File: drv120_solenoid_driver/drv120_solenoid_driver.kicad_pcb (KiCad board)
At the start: 2 copper layers, 9 parts, among them J1 Power, J2 Enable, J3 Solenoid, U1 drv120

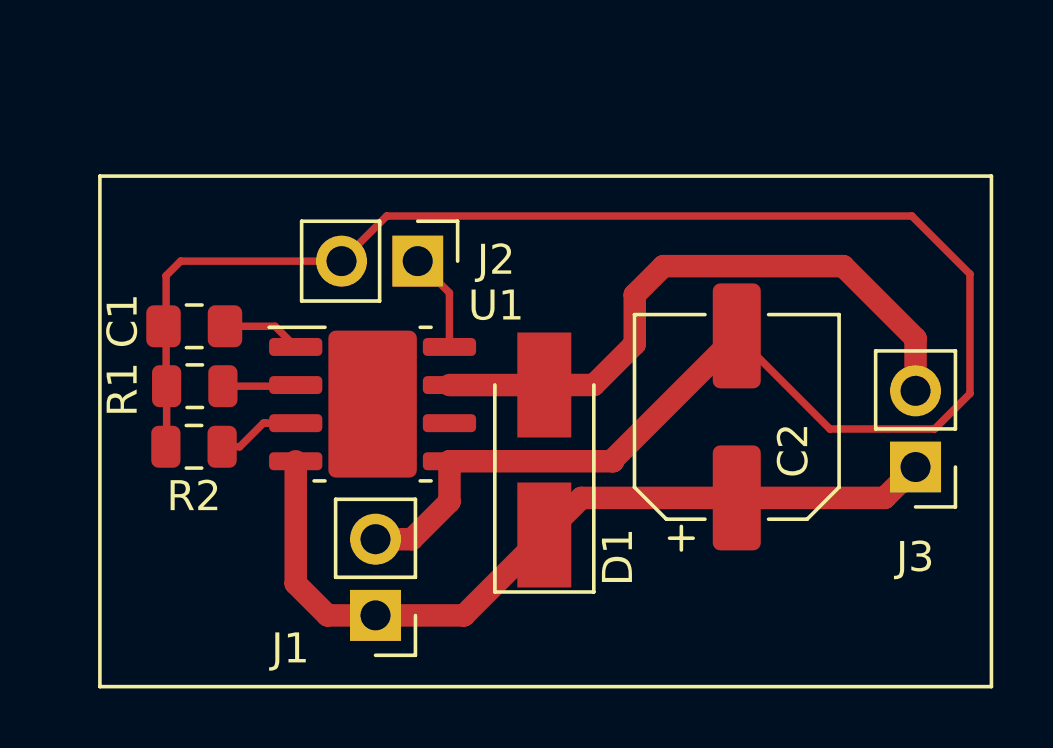
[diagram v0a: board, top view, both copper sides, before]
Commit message: Single sided for engraver
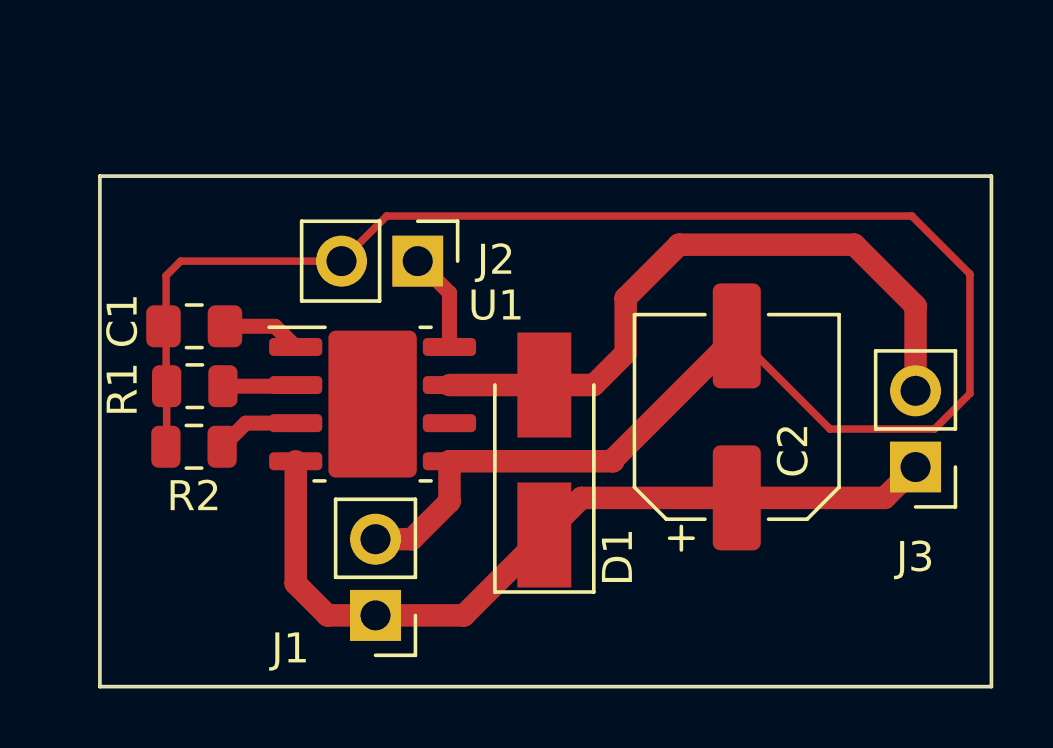
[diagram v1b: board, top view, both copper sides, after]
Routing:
- net Net-(C1-Pad1): track 2.73 -> 4.40 mm
- net Net-(D1-Pad2): track 20.9 -> 22.2 mm
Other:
- board outline added: 29.7 x 17 mm
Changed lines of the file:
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@@
   (general
     (thickness 1.6)
-    (drawings 4)
-    (tracks 48)
+    (drawings 8)
+    (tracks 47)
     (zones 0)
     (modules 9)
@@
   (layers
     (0 F.Cu signal)
-    (31 B.Cu signal)
-    (32 B.Adhes user)
-    (33 F.Adhes user)
-    (34 B.Paste user)
-    (35 F.Paste user)
+    (31 B.Cu signal hide)
+    (32 B.Adhes user hide)
+    (33 F.Adhes user hide)
+    (34 B.Paste user hide)
+    (35 F.Paste user hide)
     (36 B.SilkS user)
-    (37 F.SilkS user)
+    (37 F.SilkS user hide)
     (38 B.Mask user)
     (39 F.Mask user)
@@
   )
   (setup
-    (last_trace_width 0.25)
+    (last_trace_width 0.75)
     (user_trace_width 0.5)
     (user_trace_width 0.75)
@@
     (mod_text_size 1 1)
     (mod_text_width 0.15)
-    (pad_size 1.524 1.524)
-    (pad_drill 0.762)
+    (pad_size 3.5 1.6)
+    (pad_drill 0)
     (pad_to_mask_clearance 0.051)
     (solder_mask_min_width 0.25)
@@
     (visible_elements FFFFFF7F)
     (pcbplotparams
-      (layerselection 0x010fc_ffffffff)
+      (layerselection 0x01000_7fffffff)
       (usegerberextensions false)
       (usegerberattributes false)
@@
       (outputformat 1)
       (mirror false)
-      (drillshape 1)
+      (drillshape 0)
       (scaleselection 1)
-      (outputdirectory ""))
+      (outputdirectory "grbl/"))
   )
   (net 0 "")
@@
     (fp_line (start 3.3 -3.3) (end 3.3 3.3) (layer F.Fab) (width 0.1))
     (fp_circle (center 0 0) (end 3.15 0) (layer F.Fab) (width 0.1))
-    (pad 2 smd roundrect (at 2.7 0 90) (size 3.5 1.6) (layers F.Cu F.Paste F.Mask) (roundrect_rratio 0.15625)
-      (net 2 GND))
+    (pad 2 smd roundrect (at 2.7 0 90) (size 3.5 1.6) (layers F.Cu F.Paste F.Mask) (roundrect_rratio 0.156)
+      (net 2 GND) (zone_connect 2))
     (pad 1 smd roundrect (at -2.7 0 90) (size 3.5 1.6) (layers F.Cu F.Paste F.Mask) (roundrect_rratio 0.15625)
       (net 8 "Net-(C2-Pad1)"))
@@
     (fp_line (start -1 -0.6) (end 1 -0.6) (layer F.Fab) (width 0.1))
     (fp_line (start -1 0.6) (end -1 -0.6) (layer F.Fab) (width 0.1))
-    (pad 2 smd roundrect (at 1.025 0 180) (size 1.15 1.4) (layers F.Cu F.Paste F.Mask) (roundrect_rratio 0.217391)
-      (net 2 GND))
+    (pad 2 smd roundrect (at 1.025 0 180) (size 1.15 1.4) (layers F.Cu F.Paste F.Mask) (roundrect_rratio 0.217)
+      (net 2 GND) (zone_connect 2))
     (pad 1 smd roundrect (at -1.025 0 180) (size 1.15 1.4) (layers F.Cu F.Paste F.Mask) (roundrect_rratio 0.217391)
       (net 1 "Net-(C1-Pad1)"))
@@
     (fp_line (start -0.635 -1.27) (end 1.27 -1.27) (layer F.Fab) (width 0.1))
     (pad 2 thru_hole oval (at 0 2.54 180) (size 1.7 1.7) (drill 1) (layers *.Cu *.Mask)
-      (net 2 GND))
+      (net 2 GND) (zone_connect 2))
     (pad 1 thru_hole rect (at 0 0 180) (size 1.7 1.7) (drill 1) (layers *.Cu *.Mask)
       (net 8 "Net-(C2-Pad1)"))
@@
       (net 4 /Enable))
     (pad 2 thru_hole oval (at 0 2.54 270) (size 1.7 1.7) (drill 1) (layers *.Cu *.Mask)
-      (net 2 GND))
+      (net 2 GND) (zone_connect 2))
     (model ${KISYS3DMOD}/Connector_PinHeader_2.54mm.3dshapes/PinHeader_1x02_P2.54mm_Vertical.wrl
       (at (xyz 0 0 0))
@@
       (net 5 "Net-(R1-Pad1)"))
     (pad 2 smd roundrect (at 0.9375 0 180) (size 0.975 1.4) (layers F.Cu F.Paste F.Mask) (roundrect_rratio 0.25)
-      (net 2 GND))
+      (net 2 GND) (zone_connect 2))
     (model ${KISYS3DMOD}/Resistor_SMD.3dshapes/R_0805_2012Metric.wrl
       (at (xyz 0 0 0))
@@
     (fp_line (start -1 0.6) (end -1 -0.6) (layer F.Fab) (width 0.1))
     (pad 2 smd roundrect (at 0.9375 0 180) (size 0.975 1.4) (layers F.Cu F.Paste F.Mask) (roundrect_rratio 0.25)
-      (net 2 GND))
+      (net 2 GND) (zone_connect 2))
     (pad 1 smd roundrect (at -0.9375 0 180) (size 0.975 1.4) (layers F.Cu F.Paste F.Mask) (roundrect_rratio 0.25)
       (net 6 "Net-(R2-Pad1)"))
@@
     )
   )
+  (gr_line (start 135.382 117.602) (end 135.382 100.584) (layer Edge.Cuts) (width 0.05))
+  (gr_line (start 165.1 117.602) (end 135.382 117.602) (layer Edge.Cuts) (width 0.05))
+  (gr_line (start 165.1 100.584) (end 165.1 117.602) (layer Edge.Cuts) (width 0.05))
+  (gr_line (start 135.382 100.584) (end 165.1 100.584) (layer Edge.Cuts) (width 0.05))
   (gr_line (start 135.382 117.602) (end 135.382 100.584) (layer F.SilkS) (width 0.12))
   (gr_line (start 165.1 117.602) (end 135.382 117.602) (layer F.SilkS) (width 0.12))
   (gr_line (start 165.1 100.584) (end 165.1 117.602) (layer F.SilkS) (width 0.12))
   (gr_line (start 135.382 100.584) (end 165.1 100.584) (layer F.SilkS) (width 0.12))
-  (segment (start 141.2202 105.59034) (end 141.908981 106.279121) (width 0.25) (layer F.Cu) (net 1))
   (segment (start 139.46426 105.59034) (end 141.2202 105.59034) (width 0.25) (layer F.Cu) (net 1))
+  (segment (start 141.2202 105.59034) (end 141.908981 106.279121) (width 0.5) (layer F.Cu) (net 1))
+  (segment (start 139.55176 105.59034) (end 141.2202 105.59034) (width 0.5) (layer F.Cu) (net 1))
   (segment (start 137.58926 107.56948) (end 137.60656 107.58678) (width 0.25) (layer F.Cu) (net 2))
   (segment (start 137.58926 105.59034) (end 137.58926 107.56948) (width 0.25) (layer F.Cu) (net 2))
@@
   (segment (start 150.193559 107.549121) (end 150.19528 107.5474) (width 0.75) (layer F.Cu) (net 3))
   (segment (start 147.033981 107.549121) (end 150.193559 107.549121) (width 0.75) (layer F.Cu) (net 3))
-  (segment (start 151.84528 107.5474) (end 153.21026 106.18242) (width 0.75) (layer F.Cu) (net 3))
+  (segment (start 151.84528 107.5474) (end 152.908 106.48468) (width 0.75) (layer F.Cu) (net 3))
   (segment (start 150.19528 107.5474) (end 151.84528 107.5474) (width 0.75) (layer F.Cu) (net 3))
-  (segment (start 153.21026 106.18242) (end 153.21026 104.54132) (width 0.75) (layer F.Cu) (net 3))
-  (segment (start 154.16619 103.58539) (end 160.15881 103.58539) (width 0.75) (layer F.Cu) (net 3))
-  (segment (start 153.21026 104.54132) (end 154.16619 103.58539) (width 0.75) (layer F.Cu) (net 3))
-  (segment (start 162.57016 105.99674) (end 162.57016 107.74172) (width 0.75) (layer F.Cu) (net 3))
-  (segment (start 160.15881 103.58539) (end 162.57016 105.99674) (width 0.75) (layer F.Cu) (net 3))
-  (segment (start 147.033981 104.476281) (end 145.97634 103.41864) (width 0.25) (layer F.Cu) (net 4))
-  (segment (start 147.033981 106.279121) (end 147.033981 104.476281) (width 0.25) (layer F.Cu) (net 4))
-  (segment (start 141.871322 107.58678) (end 141.908981 107.549121) (width 0.25) (layer F.Cu) (net 5))
-  (segment (start 139.48156 107.58678) (end 141.871322 107.58678) (width 0.25) (layer F.Cu) (net 5))
-  (segment (start 140.921481 108.819121) (end 141.908981 108.819121) (width 0.25) (layer F.Cu) (net 6))
-  (segment (start 140.830619 108.819121) (end 140.921481 108.819121) (width 0.25) (layer F.Cu) (net 6))
-  (segment (start 140.04366 109.60608) (end 140.830619 108.819121) (width 0.25) (layer F.Cu) (net 6))
-  (segment (start 139.45616 109.60608) (end 140.04366 109.60608) (width 0.25) (layer F.Cu) (net 6))
+  (segment (start 152.908 106.48468) (end 152.908 104.648) (width 0.75) (layer F.Cu) (net 3))
+  (segment (start 152.908 104.648) (end 154.686 102.87) (width 0.75) (layer F.Cu) (net 3))
+  (segment (start 154.686 102.87) (end 160.528 102.87) (width 0.75) (layer F.Cu) (net 3))
+  (segment (start 162.57016 104.91216) (end 162.57016 107.74172) (width 0.75) (layer F.Cu) (net 3))
+  (segment (start 160.528 102.87) (end 162.57016 104.91216) (width 0.75) (layer F.Cu) (net 3))
+  (segment (start 147.033981 104.476281) (end 145.97634 103.41864) (width 0.5) (layer F.Cu) (net 4))
+  (segment (start 147.033981 106.279121) (end 147.033981 104.476281) (width 0.5) (layer F.Cu) (net 4))
+  (segment (start 141.871322 107.58678) (end 141.908981 107.549121) (width 0.5) (layer F.Cu) (net 5))
+  (segment (start 139.48156 107.58678) (end 141.871322 107.58678) (width 0.5) (layer F.Cu) (net 5))
+  (segment (start 140.243119 108.819121) (end 141.908981 108.819121) (width 0.5) (layer F.Cu) (net 6))
+  (segment (start 139.45616 109.60608) (end 140.243119 108.819121) (width 0.5) (layer F.Cu) (net 6))
   (segment (start 147.51558 115.2271) (end 150.19528 112.5474) (width 0.75) (layer F.Cu) (net 8))
   (segment (start 144.56918 115.2271) (end 147.51558 115.2271) (width 0.75) (layer F.Cu) (net 8))

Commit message: Double sided PCB v0.2
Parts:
- J1: value Power -> POWER
- J2: value Enable -> ENABLE
- U1: footprint Package_SO:Texas_R-PDSO-G8_EP2.95x4.9mm_Mask2.4x3.1mm -> Package_SO:TSSOP-8_4.4x3mm_P0.65mm
- moved J1 16.0 mm to (136.1, 101.6)
- moved C2 14.9 mm to (143.2, 102.1)
- moved U1 12.1 mm to (152.7, 99.3)
- moved J2 10.7 mm to (136.1, 107.7), turned to 180 degrees
- moved R2 10.5 mm to (148.9, 108.5), turned to 0 degrees
- moved J3 9.76 mm to (153.2, 107.7), turned to 90 degrees
- moved D1 7.28 mm to (152.4, 103.1), turned to 0 degrees
- moved R1 6.37 mm to (144.9, 108.5)
- moved C1 3.46 mm to (140.5, 108.5)
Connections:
- U1 pad 6: Net-(U1-Pad6) -> (no net)
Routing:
- net GND: track 63.3 -> 0.00 mm
- net /Enable: track 3.30 -> 23.4 mm, vias 0 -> 1
- net Net-(D1-Pad2): track 22.2 -> 10.3 mm
- net Net-(C1-Pad1): track 4.40 -> 15.1 mm, vias 0 -> 2
- net Net-(R1-Pad1): track 2.44 -> 12.1 mm, vias 0 -> 2
- net Net-(R2-Pad1): track 2.78 -> 10.2 mm, vias 0 -> 2
- net Net-(C2-Pad1): track 27.2 -> 25.4 mm
- added copper zone on B.Cu, net GND
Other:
- board size 29.7 x 17 mm -> 23.6 x 13 mm

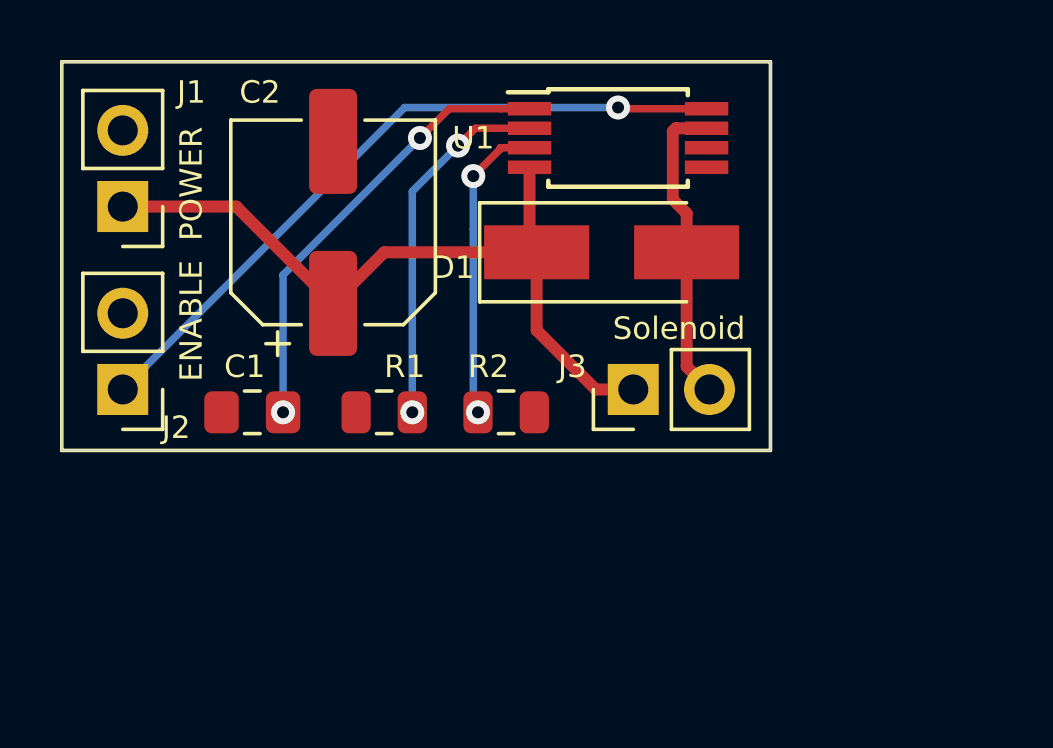
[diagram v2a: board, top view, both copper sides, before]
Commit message: Updated silk screen around connectors
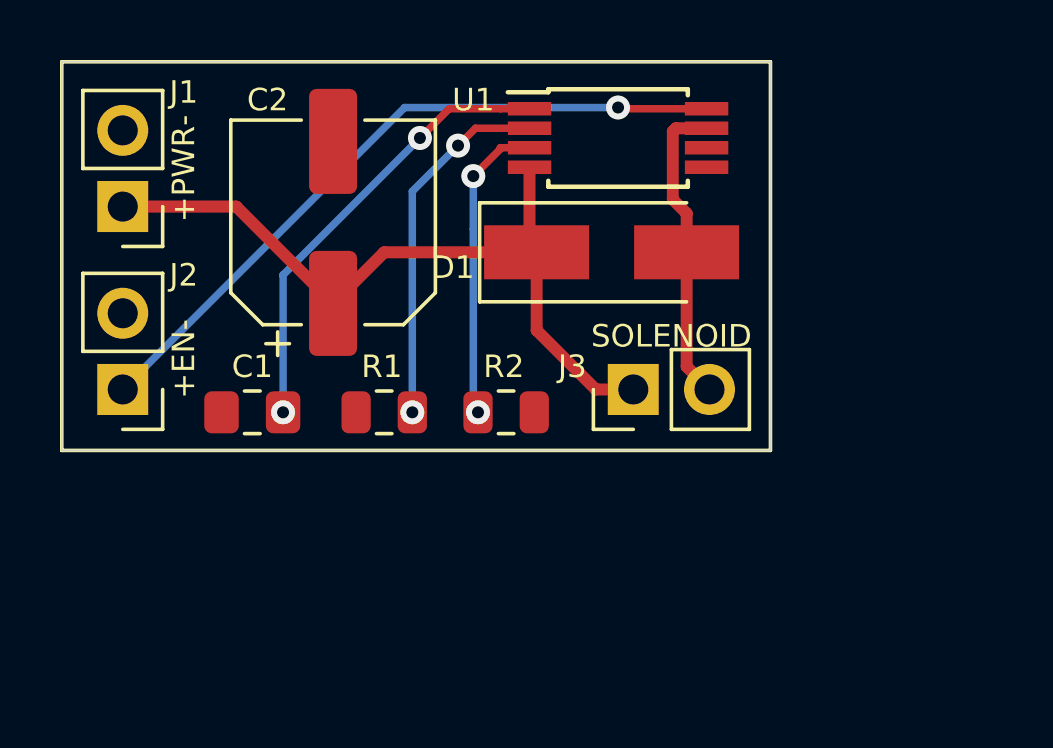
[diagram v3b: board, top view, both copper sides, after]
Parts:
- J1: value POWER -> +PWR-
- J2: value ENABLE -> +EN-
- J3: value Solenoid -> SOLENOID
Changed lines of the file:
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@@
   )
   (setup
-    (last_trace_width 0.4)
+    (last_trace_width 0.25)
     (user_trace_width 0.35)
     (user_trace_width 0.4)
@@
     (solder_mask_min_width 0.25)
     (aux_axis_origin 0 0)
-    (visible_elements FFFFFF7F)
+    (visible_elements 7FFFFFFF)
     (pcbplotparams
       (layerselection 0x010fc_ffffffff)
@@
     (add_net "Net-(R1-Pad1)")
     (add_net "Net-(R2-Pad1)")
-    (add_net "Net-(U1-Pad6)")
   )
   (module Package_SO:TSSOP-8_4.4x3mm_P0.65mm (layer F.Cu)
@@
     (tags "SSOP 0.65")
     (attr smd)
-    (fp_text reference U1 (at -4.826 0 180) (layer F.SilkS)
+    (fp_text reference U1 (at -4.826 -1.27 180) (layer F.SilkS)
       (effects (font (size 0.75 0.75) (thickness 0.1)))
     )
@@
     (tags "capacitor handsolder")
     (attr smd)
-    (fp_text reference C1 (at 0.254 1.524) (layer F.SilkS)
+    (fp_text reference C1 (at 0 1.524) (layer F.SilkS)
       (effects (font (size 0.75 0.75) (thickness 0.1)))
     )
@@
     (tags resistor)
     (attr smd)
-    (fp_text reference R2 (at -0.5865 -1.524) (layer F.SilkS)
+    (fp_text reference R2 (at -0.0785 -1.524) (layer F.SilkS)
       (effects (font (size 0.75 0.75) (thickness 0.1)))
     )
@@
     (tags resistor)
     (attr smd)
-    (fp_text reference R1 (at -0.6835 1.524) (layer F.SilkS)
+    (fp_text reference R1 (at 0.0785 1.524) (layer F.SilkS)
       (effects (font (size 0.75 0.75) (thickness 0.1)))
     )
@@
       (effects (font (size 0.75 0.75) (thickness 0.1)))
     )
-    (fp_text value Solenoid (at 2.032 1.524 180) (layer F.SilkS)
+    (fp_text value SOLENOID (at 1.778 1.27 180) (layer F.SilkS)
       (effects (font (size 0.75 0.75) (thickness 0.1)))
     )
@@
     (descr "Through hole straight pin header, 1x02, 2.54mm pitch, single row")
     (tags "Through hole pin header THT 1x02 2.54mm single row")
-    (fp_text reference J2 (at -1.778 -1.27 180) (layer F.SilkS)
-      (effects (font (size 0.75 0.75) (thickness 0.1)))
-    )
-    (fp_text value ENABLE (at -2.286 2.286 90) (layer F.SilkS)
+    (fp_text reference J2 (at -2.032 3.81 180) (layer F.SilkS)
+      (effects (font (size 0.75 0.75) (thickness 0.1)))
+    )
+    (fp_text value +EN- (at -2.032 1.016 90) (layer F.SilkS)
       (effects (font (size 0.75 0.75) (thickness 0.1)))
     )
@@
     (descr "Through hole straight pin header, 1x02, 2.54mm pitch, single row")
     (tags "Through hole pin header THT 1x02 2.54mm single row")
-    (fp_text reference J1 (at -2.286 3.81 180) (layer F.SilkS)
-      (effects (font (size 0.75 0.75) (thickness 0.1)))
-    )
-    (fp_text value POWER (at -2.286 0.762 90) (layer F.SilkS)
+    (fp_text reference J1 (at -2.032 3.81 180) (layer F.SilkS)
+      (effects (font (size 0.75 0.75) (thickness 0.1)))
+    )
+    (fp_text value +PWR- (at -2.032 1.27 90) (layer F.SilkS)
       (effects (font (size 0.75 0.75) (thickness 0.1)))
     )
@@
     (tags "capacitor electrolytic")
     (attr smd)
-    (fp_text reference C2 (at 4.337001 -2.439001 180) (layer F.SilkS)
-      (effects (font (size 0.75 0.75) (thickness 0.1)))
-    )
+    (fp_text reference C2 (at 4.083001 -2.185001 180) (layer F.SilkS)
+      (effects (font (size 0.75 0.75) (thickness 0.1)))
+    )
